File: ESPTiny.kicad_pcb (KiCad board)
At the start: 2 copper layers, 33 x 26.4 mm, 18 parts, among them J1 Conn_01x10_Male, J2 Conn_01x10_Male, J3 Conn_01x04_Male, U1 ESP-01v090, U2 ATtiny84-20PU, U3 MCP1700-3302E_TO92

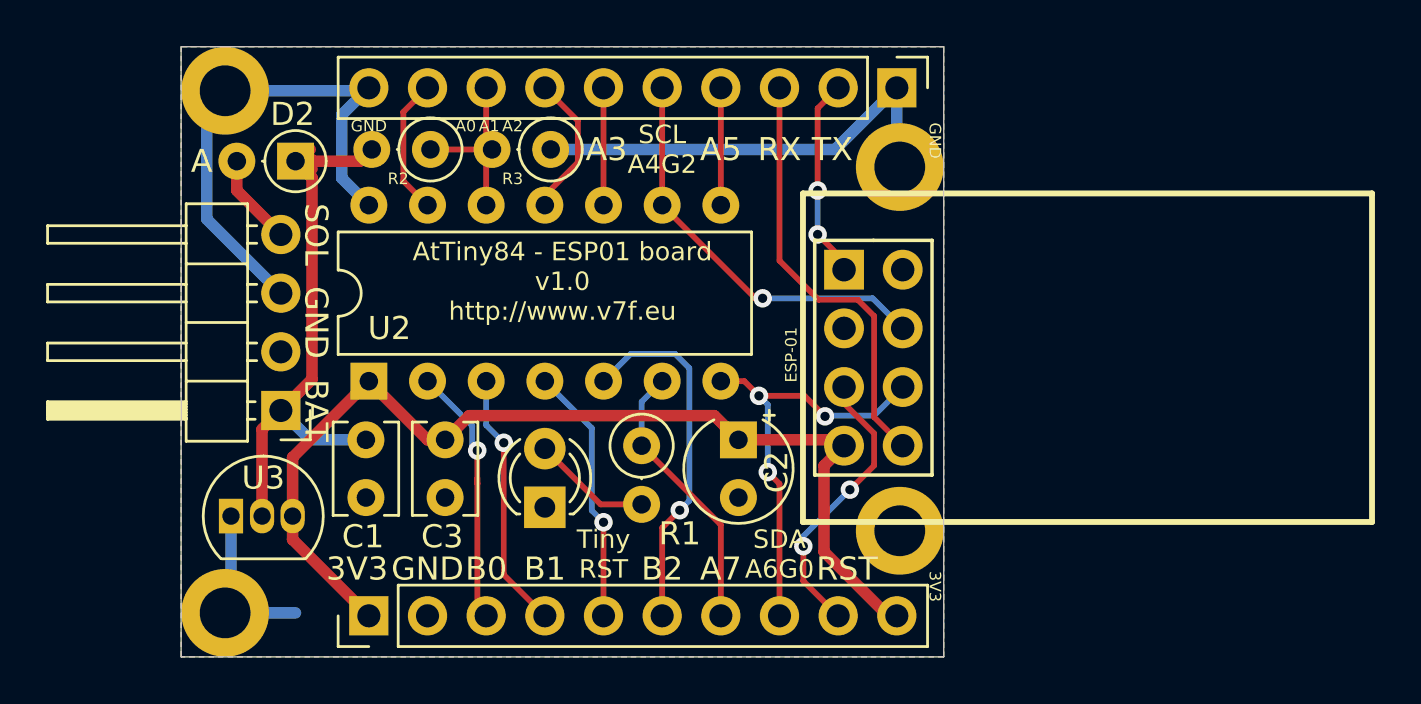
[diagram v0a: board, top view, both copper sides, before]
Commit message: Add 4k7 pull up for I2C
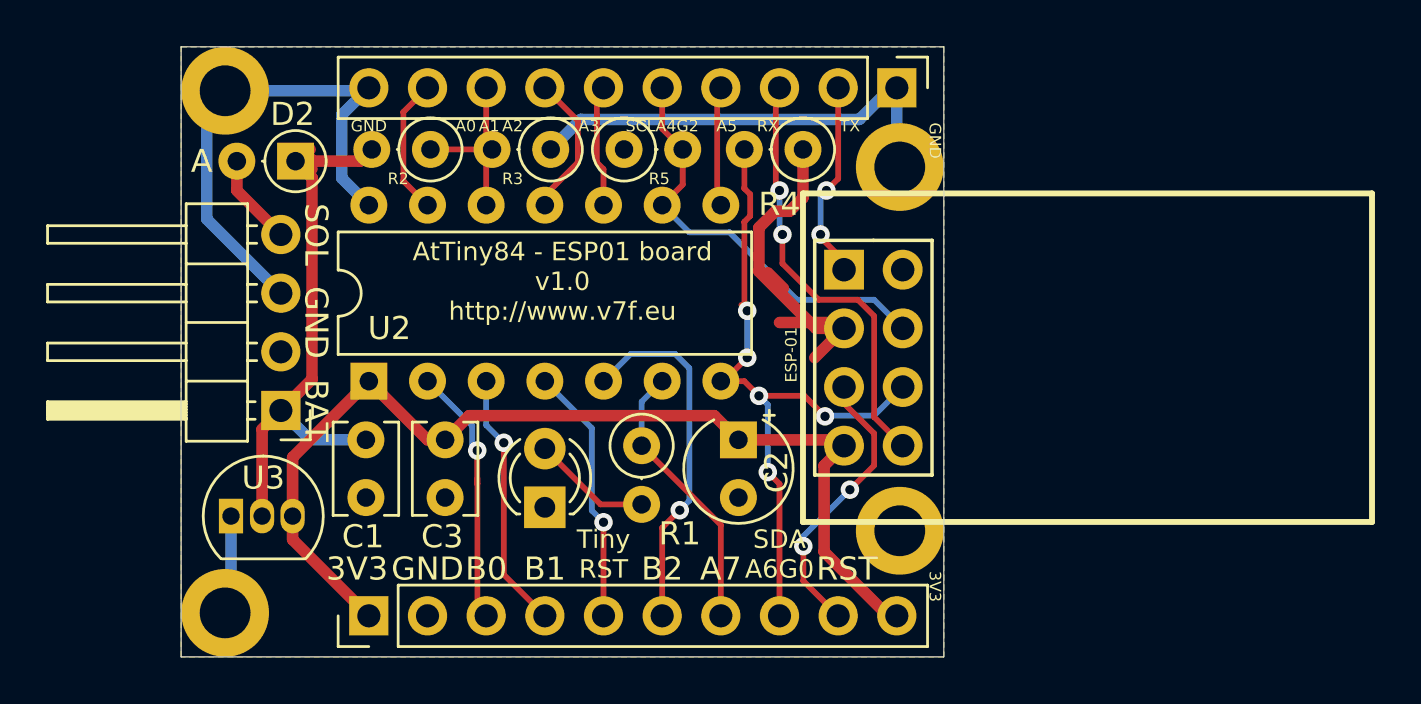
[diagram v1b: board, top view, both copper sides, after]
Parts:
- added R4: 4k7, Resistor_THT:R_Axial_DIN0207_L6.3mm_D2.5mm_P2.54mm_Vertical, F.Cu at (66.0, 44.8)
- added R5: 4k7, Resistor_THT:R_Axial_DIN0207_L6.3mm_D2.5mm_P2.54mm_Vertical, F.Cu at (58.3, 44.8)
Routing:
- net +3V3: track 45.1 -> 61.9 mm
- net /SDA-A6: track 18.9 -> 30.4 mm, vias 3 -> 5
- net GND: track 49.8 -> 46.8 mm
- net /SCL-A4: track 18.0 -> 18.4 mm, vias 1 -> 0
- net /RX: track 18.7 -> 18.9 mm, vias 0 -> 2
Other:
- board text added: "SCL-A4G2"
- board text added: "SCLA4G2"
- board text removed: "SCL A4G2"

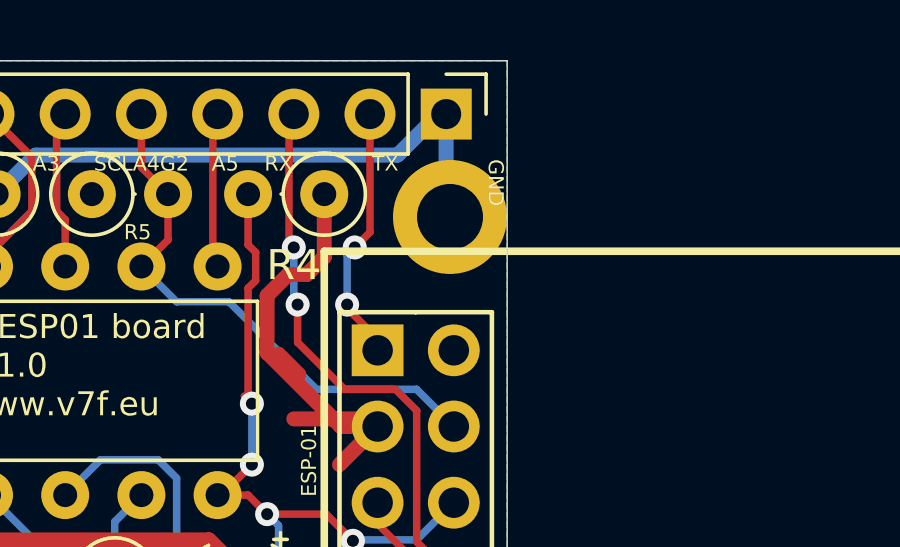
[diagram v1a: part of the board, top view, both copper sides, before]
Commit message: extra GND trace
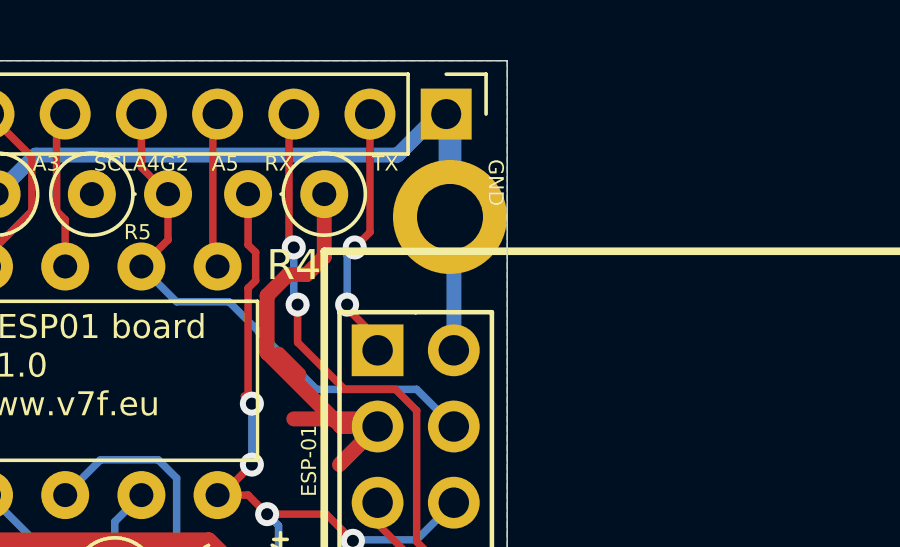
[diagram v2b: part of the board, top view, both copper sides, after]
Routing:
- net GND: track 46.8 -> 54.8 mm

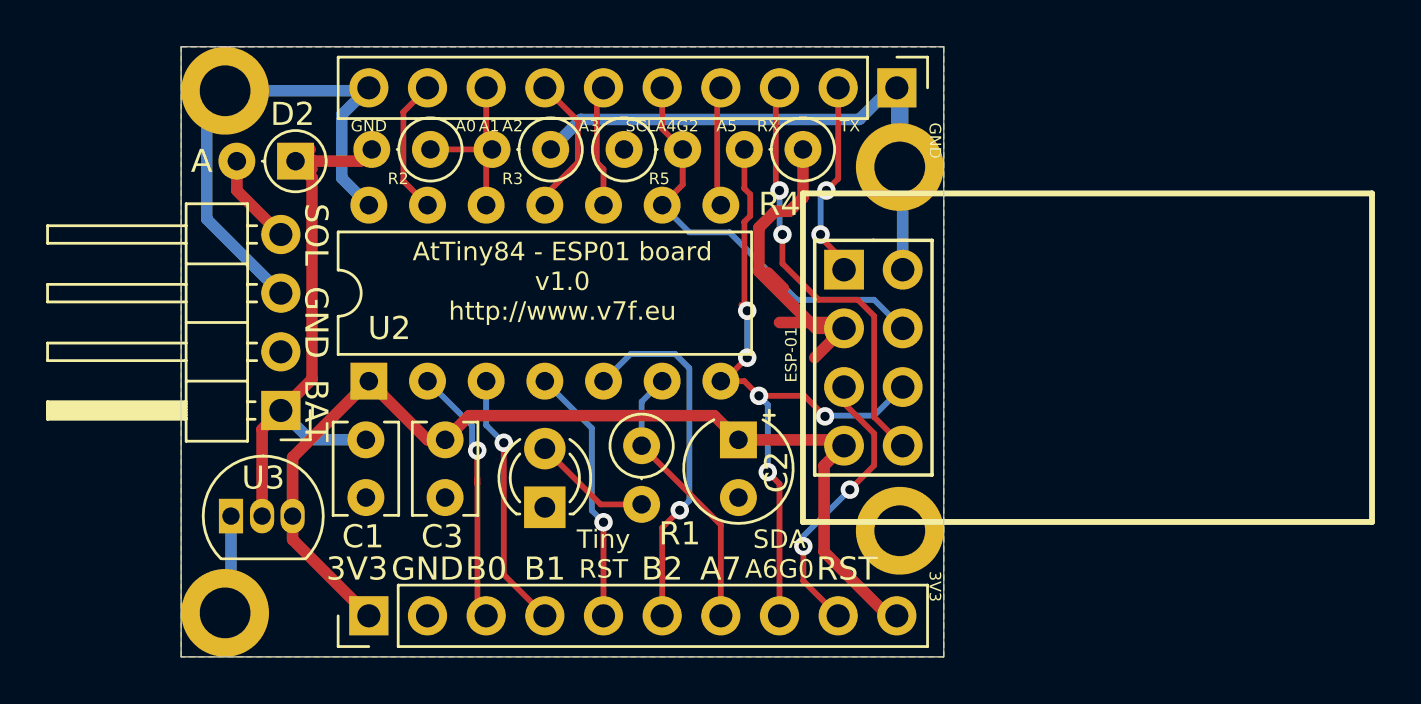
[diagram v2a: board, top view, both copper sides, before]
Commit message: Add RST jumper
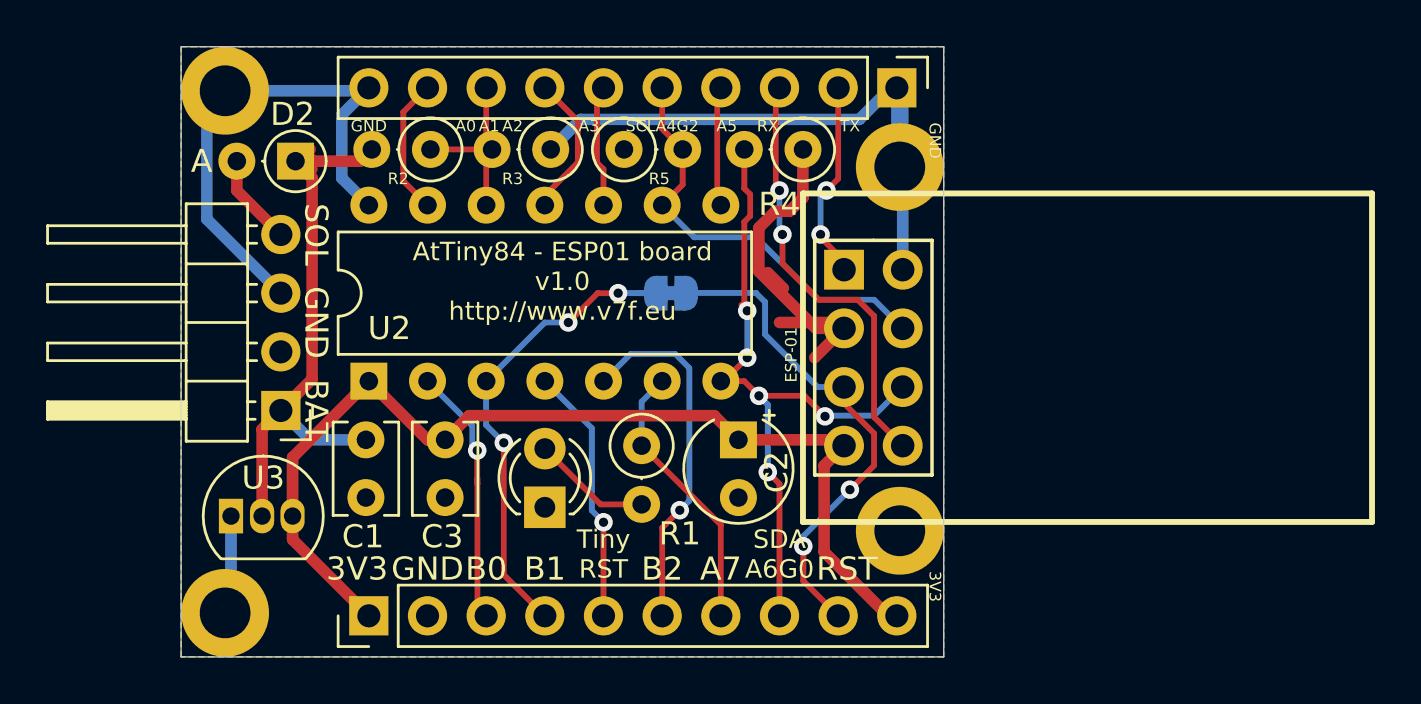
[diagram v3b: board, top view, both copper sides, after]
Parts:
- added JP1: SolderJumper_2, Jumper:SolderJumper-2_P1.3mm_Bridged_RoundedPad1.0x1.5mm, B.Cu at (60.3, 51.1)
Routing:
- net /RST: track 12.4 -> 22.0 mm
- net /B1: track 11.8 -> 21.4 mm, vias 1 -> 3

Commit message: Update 3D
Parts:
- J1, J2: moved to B.Cu
- turned J1 to 270 degrees
- turned J2 to 90 degrees

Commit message: 1.1 repositioning
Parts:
- moved D2 2.50 mm to (44.7, 42.9), turned to 270 degrees
- moved U2 0.51 mm to (47.2, 55.4)
- moved C2 0.51 mm to (63.2, 57.9)
- moved R1 0.51 mm to (59.1, 58.2)
- moved REF** 0.38 mm to (70.2, 61.7)
- moved C1 0.25 mm to (47.1, 57.7)
- moved C3 0.25 mm to (50.5, 57.7)
- moved R2 0.13 mm to (49.9, 45.0)
- moved R3 0.13 mm to (55.1, 45.0)
- moved R4 0.13 mm to (66.0, 45.0)
- moved R5 0.13 mm to (58.3, 45.0)
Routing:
- net GND: track 54.8 -> 111.0 mm
- net +3V3: track 61.9 -> 87.2 mm
- net /SDA-A6: track 30.4 -> 43.6 mm
- net /B2: track 15.7 -> 10.7 mm, vias 1 -> 0
- net /SCL-A4: track 18.4 -> 21.6 mm, vias 0 -> 2
- net /RST: track 22.0 -> 19.4 mm
- net +BATT: track 25.9 -> 27.6 mm
- net /B1: track 21.4 -> 19.8 mm, vias 3 -> 0
- net /TRST: track 11.9 -> 10.7 mm, vias 1 -> 0
- net Net-(D2-Pad2): track 4.68 -> 3.57 mm
- net /TX: track 9.02 -> 7.98 mm, vias 2 -> 0
- net /B0: track 11.4 -> 10.8 mm, vias 1 -> 0
- net /A1: track 7.96 -> 8.47 mm
- net /A3: track 5.32 -> 5.82 mm
- net /A0: track 5.95 -> 6.46 mm
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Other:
- board text added: "AtTiny84 - ESP01 board v1.1 http://www.v7f.eu"
- board text removed: "AtTiny84 - ESP01 board v1.0 http://www.v7f.eu"

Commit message: cleanup tracks
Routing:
- net +3V3: track 87.2 -> 85.8 mm

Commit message: Rev 1.2 Power bridge, layout
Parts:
- added JP2: SolderJumper_2_Open, Jumper:SolderJumper-2_P1.3mm_Open_RoundedPad1.0x1.5mm, B.Cu at (44.1, 64.5)
- moved JP1 1.52 mm to (60.3, 52.6)
- moved C1 1.14 mm to (47.1, 58.8)
- moved C3 1.14 mm to (50.5, 58.8)
- moved R4 1.05 mm to (65.8, 46.0)
- moved R5 1.02 mm to (58.4, 46.0)
- moved R1 1.02 mm to (59.1, 59.2)
- moved C2 1.02 mm to (63.2, 58.9)
- moved D1 1.02 mm to (54.9, 61.3)
- moved R2 1.02 mm to (49.9, 46.0)
- moved R3 1.02 mm to (55.1, 46.0)
- moved U2 1.02 mm to (47.2, 56.4)
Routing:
- net GND: track 111.0 -> 65.3 mm
- net +3V3: track 85.8 -> 41.6 mm
- net /SDA-A6: track 43.6 -> 34.4 mm, vias 5 -> 2
- net /A5: track 5.72 -> 9.11 mm
- net +BATT: track 27.6 -> 29.4 mm
- net /B1: track 19.8 -> 18.6 mm
- net /B0: track 10.8 -> 9.74 mm
- net /TRST: track 10.7 -> 9.69 mm
- net /B2: track 10.7 -> 9.69 mm
- net /A7: track 11.4 -> 10.4 mm
- net /A2: track 6.35 -> 7.37 mm
- net /A1: track 8.47 -> 9.48 mm
- net /A0: track 6.46 -> 7.47 mm
- net /A3: track 5.82 -> 6.84 mm
- net /RST: track 19.4 -> 19.0 mm, vias 2 -> 3
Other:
- board text added: "AtTiny84 - ESP01 board v1.2 http://www.v7f.eu"
- board text added: "SCL A4G2"
- board text removed: "AtTiny84 - ESP01 board v1.1 http://www.v7f.eu"
- board text removed: "SCL-A4G2"
- board text removed: "SCLA4G2"

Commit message: cleanup tracks
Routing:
- net GND: track 65.3 -> 57.6 mm
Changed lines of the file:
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@@
     (thickness 1.6)
     (drawings 49)
-    (tracks 171)
+    (tracks 167)
     (zones 0)
     (modules 22)
@@
   (layers
     (0 F.Cu signal)
-    (31 B.Cu signal hide)
+    (31 B.Cu signal)
     (32 B.Adhes user)
     (33 F.Adhes user)
@@
   (segment (start 49.784 65.024) (end 50.927 66.167) (width 0.5) (layer B.Cu) (net 1) (status 10))
   (segment (start 70.231 61.722) (end 70.485 61.722) (width 0.5) (layer B.Cu) (net 1) (status 30))
-  (segment (start 70.358 50.038) (end 71.374 49.022) (width 0.5) (layer B.Cu) (net 1))
-  (segment (start 70.358 50.038) (end 69.342 49.022) (width 0.5) (layer B.Cu) (net 1))
-  (segment (start 70.358 50.038) (end 71.247 50.927) (width 0.5) (layer B.Cu) (net 1))
-  (segment (start 43.434 51.054) (end 45.974 48.514) (width 0.5) (layer B.Cu) (net 1))
   (segment (start 63.246 57.550002) (end 63.246 58.928) (width 0.5) (layer F.Cu) (net 2) (status 20))
   (segment (start 67.818 52.578) (end 67.818 52.978002) (width 0.5) (layer F.Cu) (net 2) (status 30))
@@
   (segment (start 58.42 45.344103) (end 59.526112 44.237991) (width 0.5) (layer F.Cu) (net 2) (status 10))
   (segment (start 58.42 45.974) (end 58.42 45.344103) (width 0.5) (layer F.Cu) (net 2) (status 30))
-  (segment (start 47.102 65.166) (end 47.244 65.024) (width 0.5) (layer B.Cu) (net 2))
-  (segment (start 44.1452 65.166) (end 47.102 65.166) (width 0.5) (layer B.Cu) (net 2))
+  (segment (start 47.102 65.166) (end 47.244 65.024) (width 0.5) (layer B.Cu) (net 2) (status 30))
+  (segment (start 44.1452 65.166) (end 47.102 65.166) (width 0.5) (layer B.Cu) (net 2) (status 30))
   (segment (start 43.434 46.736) (end 44.704 45.466) (width 0.5) (layer F.Cu) (net 3) (status 20))
   (segment (start 43.434 48.514) (end 43.434 46.736) (width 0.5) (layer F.Cu) (net 3) (status 10))
@@
   (segment (start 44.704 43.307) (end 47.371 45.974) (width 0.5) (layer F.Cu) (net 5) (status 30))
   (segment (start 44.704 42.926) (end 44.704 43.307) (width 0.5) (layer F.Cu) (net 5) (status 30))
-  (segment (start 42.6212 62.342) (end 44.1452 63.866) (width 0.5) (layer B.Cu) (net 5))
-  (segment (start 42.6212 60.706) (end 42.6212 62.342) (width 0.5) (layer B.Cu) (net 5))
+  (segment (start 42.6212 62.342) (end 44.1452 63.866) (width 0.5) (layer B.Cu) (net 5) (status 20))
+  (segment (start 42.6212 60.706) (end 42.6212 62.342) (width 0.5) (layer B.Cu) (net 5) (status 10))
   (segment (start 52.324 58.839998) (end 52.324 65.024) (width 0.25) (layer F.Cu) (net 6) (status 20))
   (segment (start 49.872002 56.388) (end 52.324 58.839998) (width 0.25) (layer F.Cu) (net 6) (status 10))
